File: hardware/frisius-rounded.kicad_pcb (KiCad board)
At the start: 4 copper layers, 50 x 50 mm, 117 parts, among them Q1 Q_NMOS_DGS, Q2 MBT2222ADW1T1, SW1 OVERRIDE, SW4 SW_Push, U1 ESP32-PICO-V3-02, U10 CP2102N-Axx-xQFN24, U12 RT5789, U2 FXOS8700CQR1, U3 MS5637-02BA03, U4 L96-M33, U5 MAX77751, U6 LM75B, U7 MAX17048G

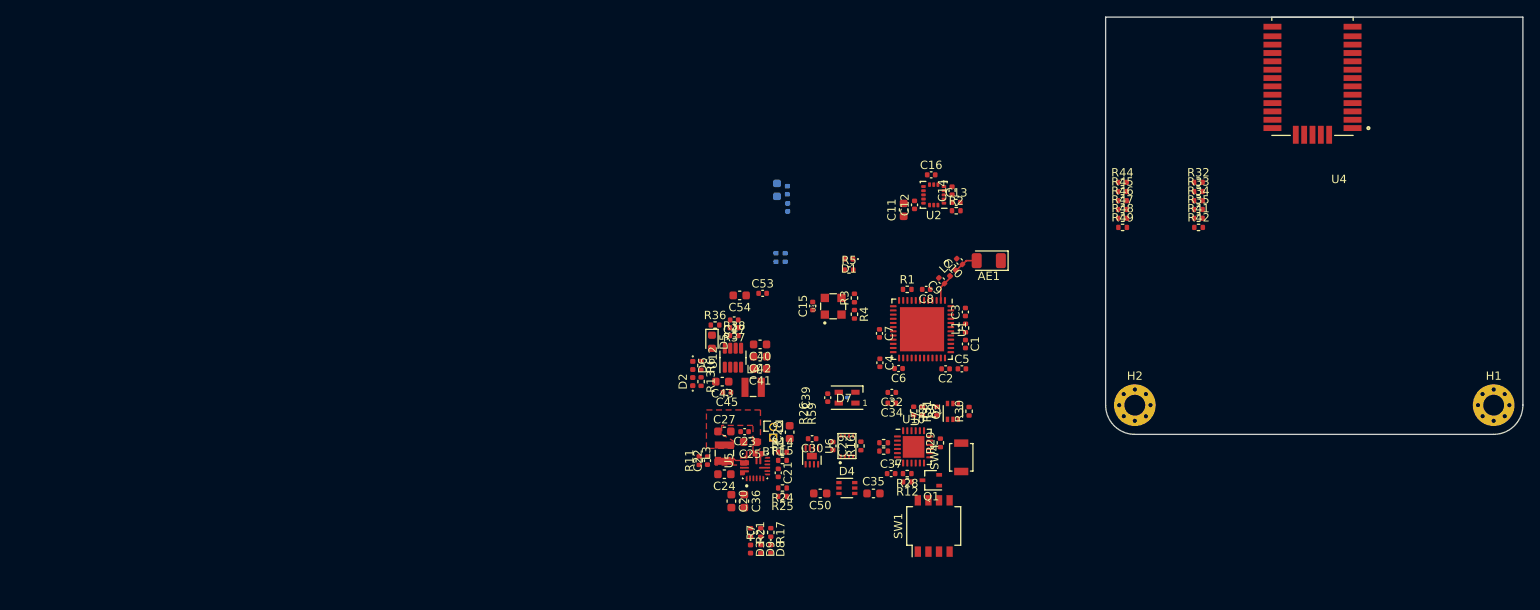
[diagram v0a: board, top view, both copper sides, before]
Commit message: layout 0 unconnected
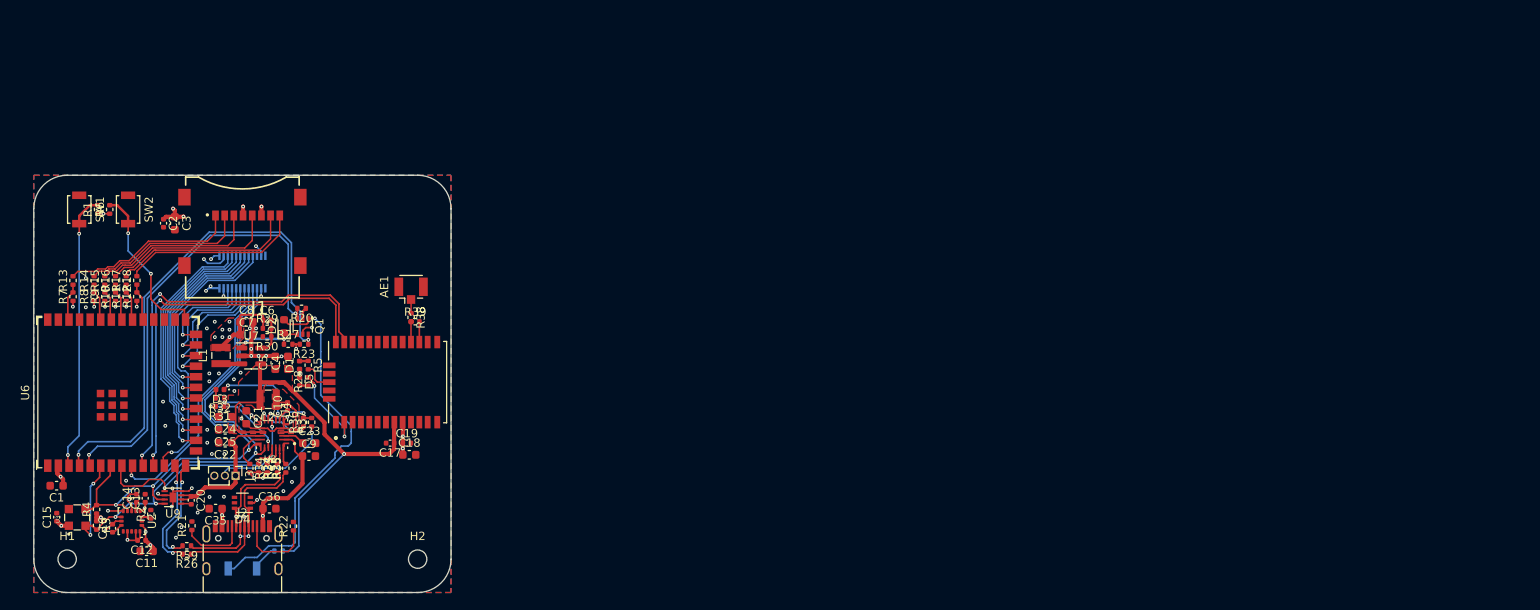
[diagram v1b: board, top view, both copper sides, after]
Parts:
- removed BT1: JST-PH-2, Connector_PinHeader_1.27mm:PinHeader_1x02_P1.27mm_Vertical
- removed C27, C28, C40, C41, C42: 10u, Capacitor_SMD:C_0603_1608Metric
- removed C29, C30, C37, C39, C53: 0.1u, Capacitor_SMD:C_0402_1005Metric
- removed C32, C34, C45: 1u, Capacitor_SMD:C_0402_1005Metric
- removed C43, C50, C54: 4.7u, Capacitor_SMD:C_0603_1608Metric
- removed C47: 10p, Capacitor_SMD:C_0402_1005Metric
- removed D6, D8, D9: LED_Small_Filled, LED_SMD:LED_0402_1005Metric
- removed D7: SK6805, LED_SMD:LED_SK6805_PLCC4_2.4x2.7mm_P1.3mm
- removed L3: 0.47u, Inductor_SMD:L_Wuerth_MAPI-2510
- removed L4: 1u, Inductor_SMD:L_Wuerth_MAPI-2510
- removed Q2: MBT2222ADW1T1, Package_TO_SOT_SMD:SOT-363_SC-70-6
- removed R41, R42: 22, Resistor_SMD:R_0402_1005Metric
- removed R44, R45, R46, R47, R48, R49: 10k, Resistor_SMD:R_0402_1005Metric
- removed SW4: SW_Push, Button_Switch_SMD:SW_SPST_B3U-1000P
- removed U1: ESP32-PICO-V3-02, Package_DFN_QFN:QFN-48-1EP_7x7mm_P0.5mm_EP5.3x5.3mm
- removed U10: CP2102N-Axx-xQFN24, Package_DFN_QFN:QFN-24-1EP_4x4mm_P0.5mm_EP2.6x2.6mm
- removed U12: RT5789, Package_TO_SOT_SMD:TSOT-23-8
- removed U5: MAX77751, bt_Package_QFN:FC2QFN-24-3x3_P0.4mm
- added J1: MEM2067, bt_Connector_uSD:GCT_MEM2067-02-180-00-A_REVB, F.Cu at (71.6, 90.9)
- added J2: USB_C_Receptacle_USB2.0, Connector_USB:USB_C_Receptacle_HRO_TYPE-C-31-M-12, F.Cu at (71.6, 129.6)
- added J3: BATTERY, Connector_PinHeader_1.27mm:PinHeader_1x03_P1.27mm_Vertical, F.Cu at (70.7, 119.5)
- added J4: Display, Connector_Molex:Molex_SlimStack_55560-0241_2x12_P0.50mm_Vertical, B.Cu at (71.6, 95.0)
- added R10: 10k, Resistor_SMD:R_0402_1005Metric, F.Cu at (56.4, 98.0)
- added R18: 22, Resistor_SMD:R_0402_1005Metric, F.Cu at (58.9, 96.0)
- added R19: 100k, Resistor_SMD:R_0402_1005Metric, B.Cu at (75.9, 128.5)
- added R20: 100k, Resistor_SMD:R_0402_1005Metric, F.Cu at (78.7, 99.4)
- added R22: 0, Resistor_SMD:R_0402_1005Metric, F.Cu at (77.7, 125.5)
- added R39: 0, Resistor_SMD:R_0402_1005Metric, F.Cu at (92.3, 101.0)
- added SW2: BOOT, Button_Switch_SMD:SW_SPST_B3U-1000P, F.Cu at (57.9, 87.5)
- added SW3: POWER, Button_Switch_SMD:SW_SPST_B3U-1000P, B.Cu at (71.6, 130.6)
- added U8: MP2723, bt_Package_QFN:MP_QFN-26-3.5x3.5_P0.45mm, F.Cu at (75.1, 114.5)
- added U9: MAX17048G, Package_DFN_QFN:TDFN-8-1EP_2x2mm_P0.5mm_EP0.8x1.2mm, F.Cu at (63.2, 122.0)
- AE1: value 2.4G -> Antenna_Shield; footprint RF_Antenna:Johanson_2450AT18x100 -> Connector_Coaxial:U.FL_Hirose_U.FL-R-SMT-1_Vertical
- C1, C3, C5, C9: value 0.1u -> 4.7u; footprint Capacitor_SMD:C_0402_1005Metric -> Capacitor_SMD:C_0603_1608Metric
- C17, C18, C19: moved to F.Cu
- C2: value 1u -> 0.1u
- C20: value 4.7u -> 0.1u; footprint Capacitor_SMD:C_0603_1608Metric -> Capacitor_SMD:C_0402_1005Metric
- C21, C23: value 1u -> 10u; footprint Capacitor_SMD:C_0402_1005Metric -> Capacitor_SMD:C_0603_1608Metric
- C22, C7, C8: value 0.1u -> 10u; footprint Capacitor_SMD:C_0402_1005Metric -> Capacitor_SMD:C_0603_1608Metric
- C4: value 1u -> 4.7u; footprint Capacitor_SMD:C_0402_1005Metric -> Capacitor_SMD:C_0603_1608Metric
- C6: value 0.1u -> 10p
- D2: value LED_Small_Filled -> MBR0540; footprint LED_SMD:LED_0402_1005Metric -> LED_SMD:LED_0603_1608Metric
- D5: value MBR0540 -> LED_Small_Filled; footprint LED_SMD:LED_0603_1608Metric -> LED_SMD:LED_0402_1005Metric
- H1, H2: footprint MountingHole:MountingHole_2.5mm_Pad_Via -> MountingHole:MountingHole_2.2mm_M2_ISO7380
- L1: value 0 -> 1u; footprint Resistor_SMD:R_0402_1005Metric -> Inductor_SMD:L_Wuerth_MAPI-2510
- L2: value L_Small -> 0.47u; footprint Inductor_SMD:L_0402_1005Metric -> Inductor_SMD:L_Wuerth_MAPI-2510
- N6: footprint Fiducial:Fiducial_0.5mm_Mask1.5mm -> Symbol:WEEE-Logo_4.2x6mm_SilkScreen
- Q1: value Q_NMOS_DGS -> Q_Dual_NMOS_G1S2G2D2S1D1; footprint Package_TO_SOT_SMD:SOT-323_SC-70 -> Package_TO_SOT_SMD:SOT-363_SC-70-6
- R1: value 100k -> R_Small
- R11, R12: value 100k -> 10k
- R13, R17: value 1k -> 22
- R14, R15: value 14k -> 22
- R16: value 0 -> 22
- R21: value 1k -> 0
- R23, R27: value 0 -> 100k; moved to F.Cu
- R28: value 100k -> 1k
- R29: value 100k -> ?
- R30: value 10k -> 100k
- R31: value 10k -> 1k
- R32: value 22 -> 1k
- R33, R34: value 22 -> 0
- R35: value 22 -> 14k
- R36: value 100k -> 14k
- R37: value ? -> 14k
- R38: value 100k -> 0
- R6: value 1k -> R_Small
- R7: value 1k -> 10k
- R8, R9: value 0 -> 10k
- SW1: value OVERRIDE -> RESET; footprint Button_Switch_SMD:SW_DIP_SPSTx04_Slide_Omron_A6H-4101_W6.15mm_P1.27mm -> Button_Switch_SMD:SW_SPST_B3U-1000P
- U6: value LM75B -> ESP32-S3-WROOM-1; footprint bt_Package_SON:XSON-8U -> bt_Espressif:ESP32-S3-WROOM-1U
- U7: value MAX17048G -> TLV62569DBV; footprint Package_DFN_QFN:TDFN-8-1EP_2x2mm_P0.5mm_EP0.8x1.2mm -> Package_TO_SOT_SMD:SOT-23-5
- moved H1 171.9 mm to (50.6, 129.4)
- moved R32 120.1 mm to (68.9, 110.2), turned to 180 degrees
- moved R34 118.1 mm to (72.5, 118.5), turned to -90 degrees
- moved R33 117.4 mm to (73.5, 118.5), turned to -90 degrees
- moved U4 116.7 mm to (89.0, 108.2), turned to 90 degrees
- moved R35 115.8 mm to (74.5, 118.6), turned to -90 degrees
- moved C1 110.2 mm to (49.3, 120.7), turned to 180 degrees
- moved SW1 109.2 mm to (52.0, 87.5), turned to -90 degrees
- moved C16 106.9 mm to (56.0, 125.8), turned to 90 degrees
- moved C14 104.4 mm to (58.9, 122.2)
- moved U2 103.8 mm to (58.3, 124.9), turned to -90 degrees
- moved C13 103.5 mm to (59.9, 122.2), turned to 90 degrees
- moved R2 103.1 mm to (60.6, 124.1), turned to 90 degrees
- moved N6 102.8 mm to (238.1, 68.7)
- moved C12 101.0 mm to (59.5, 127.2), turned to 180 degrees
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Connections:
- net /USB/PORT_D+ renamed /Power/PORT_D+
- net /USB/PORT_D- renamed /Power/PORT_D-
- AE1 pad 1: unconnected-(AE1-Pad1) -> /GPS/ANT_RF
- AE1 pad 2: Net-(AE1-Pad2) -> GND
- C1 pad 1: VDD_CORE_3V3 -> +3V3
- C10 pad 1: Net-(AE1-Pad2) -> Net-(C10-Pad1)
- C10 pad 2: GND -> Net-(C10-Pad2)
- C11 pad 1: VDD_AUX_3V3 -> +3V3
- C12 pad 1: VDD_AUX_3V3 -> +3V3
- C13 pad 1: Net-(C13-Pad1) -> +3V3
- C15 pad 1: VDD_AUX_3V3 -> +3V3
- C18 pad 1: VDD_AUX_3V3 -> +3V3
- C19 pad 1: VDD_AUX_3V3 -> +3V3
- C2 pad 1: VDD_CORE_3V3 -> +3V3
- C20 pad 1: VBUS -> +BATT
- C21 pad 1: Net-(C21-Pad1) -> /Power/VREF
- C22 pad 1: Net-(C22-Pad1) -> +BATT
- C22 pad 2: Net-(C22-Pad2) -> GND
- C24 pad 1: VBUS_OVP -> VDD_NVDC
- C3 pad 1: /Processor/3V3_ESP_VDDA_FILT -> +3V3
- C4 pad 1: VDD_CORE_3V3 -> VDD_NVDC
- C5 pad 1: VDD_CORE_3V3 -> VDD_NVDC
- C6 pad 1: Net-(C6-Pad1) -> +3V3
- C6 pad 2: GND -> Net-(C6-Pad2)
- C7 pad 1: VDD_CORE_3V3 -> +3V3
- C8 pad 1: /Processor/3V3_ESP_VDDA_FILT -> +3V3
- C9 pad 1: Net-(C9-Pad1) -> VBUS
- D2 pad 2: VDD_NVDC -> Net-(D2-Pad2)
- D3 pad 2: VDD_NVDC -> Net-(D3-Pad2)
- D4 pad 3: /BMS/USB_CC.1 -> unconnected-(D4-Pad3)
- D4 pad 4: /BMS/USB_CC.2 -> unconnected-(D4-Pad4)
- D5 pad 1: /Power/POWER_EN -> GND
- D5 pad 2: /Power/BOOTSTRAP -> Net-(D5-Pad2)
- L1 pad 1: VDD_CORE_3V3 -> Net-(L1-Pad1)
- L1 pad 2: /Processor/3V3_ESP_VDDA_FILT -> +3V3
- L2 pad 1: Net-(C9-Pad1) -> Net-(C10-Pad2)
- L2 pad 2: Net-(AE1-Pad2) -> VDD_NVDC
- Q1 pad 1: /Processor/USB_PRESENT -> Net-(D2-Pad2)
- Q1 pad 2: Net-(Q1-Pad2) -> GND
- Q1 pad 3: GND -> /Power/SHUTDOWN
- R1 pad 1: VDD_CORE_3V3 -> +3V3
- R1 pad 2: /Processor/DEV_BTN.RST -> /Processor/RST_BTN
- R11 pad 1: Net-(Q1-Pad2) -> +3V3
- R11 pad 2: VDD_NVDC -> /Processor/SDMMC.D0
- R12 pad 1: /Processor/USB_PRESENT -> +3V3
- R12 pad 2: VDD_CORE_3V3 -> /Processor/SDMMC.D1
- R13 pad 1: Net-(Q1-Pad2) -> /Processor/SDMMC.D2
- R13 pad 2: Net-(D2-Pad1) -> Net-(J1-Pad1)
- R14 pad 1: Net-(R14-Pad1) -> /Processor/SDMMC.D3
- R14 pad 2: GND -> Net-(J1-Pad2)
- R15 pad 1: Net-(R15-Pad1) -> /Processor/SDMMC.CMD
- R15 pad 2: GND -> Net-(J1-Pad3)
- R16 pad 1: /BMS/THERM_SHDN -> /Processor/SDMMC.CLK
- R16 pad 2: Net-(R15-Pad1) -> Net-(J1-Pad5)
- R17 pad 1: Net-(D8-Pad1) -> /Processor/SDMMC.D0
- R21 pad 2: Net-(D3-Pad1) -> GND
- R23 pad 1: Net-(R23-Pad1) -> /Power/POWER_BUTTON
- R23 pad 2: /BMS/SENSOR_I2C.SDA -> +3V3
- R24 pad 2: /BMS/USB_CHG.D- -> /Power/USB_CHG.D-
- R25 pad 2: /BMS/USB_CHG.D+ -> /Power/USB_CHG.D+
- R26 pad 2: /USB/CP2102N_D- -> /Power/USB_ESP.D-
- R27 pad 1: Net-(R27-Pad1) -> Net-(D2-Pad1)
- R27 pad 2: /BMS/SENSOR_I2C.SCL -> +3V3
- R28 pad 1: Net-(R28-Pad1) -> Net-(D5-Pad2)
- R28 pad 2: VDD_CORE_3V3 -> /GPS/L96_FIX
- R29 pad 1: /USB/CP2102N_~{SUS} -> +3V3
- R29 pad 2: GND -> Net-(C6-Pad2)
- R3 pad 1: VDD_AUX_3V3 -> +3V3
- R3 pad 2: /BMS/SENSOR_I2C.SDA -> /Display/SYS_I2C.SDA
- R30 pad 1: /USB/~{RTS}_BASE -> Net-(C6-Pad2)
- R30 pad 2: /USB/CP2102N_RTS -> GND
- R31 pad 1: /USB/CP2102N_DTR -> /Power/VREF
- R31 pad 2: /USB/DTR_BASE -> Net-(R31-Pad2)
- R32 pad 1: /Processor/SDMMC.D2 -> /Power/VREF
- R32 pad 2: Net-(J4-Pad1) -> Net-(D3-Pad2)
- R33 pad 1: /Processor/SDMMC.D3 -> Net-(R33-Pad1)
- R33 pad 2: Net-(J4-Pad2) -> GND
- R34 pad 1: /Processor/SDMMC.CMD -> Net-(R34-Pad1)
- R34 pad 2: Net-(J4-Pad3) -> GND
- R35 pad 1: /Processor/SDMMC.CLK -> Net-(R35-Pad1)
- R35 pad 2: Net-(J4-Pad5) -> GND
- R36 pad 1: /Power/POWER_EN -> Net-(R36-Pad1)
- R36 pad 2: VDD_SYS_3V5 -> Net-(R36-Pad2)
- R37 pad 1: VDD_SYS_3V5 -> Net-(J3-Pad2)
- R37 pad 2: Net-(C47-Pad2) -> Net-(R36-Pad2)
- R38 pad 1: Net-(C47-Pad2) -> /GPS/ANT_RF
- R38 pad 2: GND -> /GPS/GPS_RF
- R4 pad 1: VDD_AUX_3V3 -> +3V3
- R4 pad 2: /BMS/SENSOR_I2C.SCL -> /Display/SYS_I2C.SCL
- R59 pad 2: /USB/CP2102N_D+ -> /Power/USB_ESP.D+
- R6 pad 1: Net-(D6-Pad1) -> +3V3
- R6 pad 2: Net-(R6-Pad2) -> /Processor/BOOT_BTN
- R7 pad 1: Net-(D9-Pad1) -> +3V3
- R7 pad 2: Net-(R7-Pad2) -> /Processor/SDMMC.D2
- R8 pad 1: /Processor/DEBUG_UART.RXD -> +3V3
- R8 pad 2: /USB/CP2102N_UART_TX -> /Processor/SDMMC.D3
- R9 pad 1: /Processor/DEBUG_UART.TXD -> +3V3
- R9 pad 2: /USB/CP2102N_UART_RX -> /Processor/SDMMC.CMD
- SW1 pad 1: unconnected-(SW1-Pad1) -> GND
- SW1 pad 2: unconnected-(SW1-Pad2) -> /Processor/RST_BTN
- U2 pad 1: Net-(C13-Pad1) -> +3V3
- U2 pad 14: VDD_AUX_3V3 -> +3V3
- U2 pad 4: /BMS/SENSOR_I2C.SCL -> /Display/SYS_I2C.SCL
- U2 pad 6: /BMS/SENSOR_I2C.SDA -> /Display/SYS_I2C.SDA
- U3 pad 1: VDD_AUX_3V3 -> +3V3
- U3 pad 2: /BMS/SENSOR_I2C.SDA -> /Display/SYS_I2C.SDA
- U3 pad 3: /BMS/SENSOR_I2C.SCL -> /Display/SYS_I2C.SCL
- U4 pad 16: /GPS/GPS_RF -> /GPS/MOD_RF
- U4 pad 2: Net-(TP11-Pad1) -> /GPS/L96_FIX
- U4 pad 3: Net-(R23-Pad1) -> unconnected-(U4-Pad3)
- U4 pad 6: Net-(R27-Pad1) -> unconnected-(U4-Pad6)
- U4 pad 9: VDD_AUX_3V3 -> +3V3
- U6 pad 1: /BMS/SENSOR_I2C.SDA -> GND
- U6 pad 2: /BMS/SENSOR_I2C.SCL -> +3V3
- U6 pad 3: /BMS/THERM_SHDN -> /Processor/RST_BTN
- U6 pad 4: GND -> /Power/POWER_BUTTON
- U6 pad 5: GND -> /Power/SHUTDOWN
- U6 pad 6: GND -> /Display/SYS_I2C.SDA
- U6 pad 7: GND -> /Display/SYS_I2C.SCL
- U6 pad 8: +BATT -> /Power/BMS_INT
- U7 pad 1: GND -> Net-(D2-Pad1)
- U7 pad 2: +BATT -> GND
- U7 pad 3: +BATT -> Net-(L1-Pad1)
- U7 pad 4: GND -> VDD_NVDC
- U7 pad 5: unconnected-(U7-Pad5) -> Net-(C6-Pad2)
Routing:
- net /Display/SYS_I2C.SDA: track 0.00 -> 65.2 mm, vias 0 -> 5
- net /Power/POWER_BUTTON: track 0.00 -> 61.9 mm, vias 0 -> 2
- net /Display/SYS_I2C.SCL: track 0.00 -> 59.4 mm, vias 0 -> 3
- net /Power/SHUTDOWN: track 0.00 -> 56.1 mm, vias 0 -> 2
- net GND: track 0.00 -> 53.6 mm, vias 0 -> 53
- net VDD_NVDC: track 0.00 -> 52.7 mm, vias 0 -> 1
- net /GPS/GPS_UART.RX: track 0.00 -> 48.9 mm, vias 0 -> 2
- net /GPS/GPS_UART.TX: track 0.00 -> 46.6 mm, vias 0 -> 2
- net Net-(D2-Pad2): track 0.00 -> 45.7 mm, vias 0 -> 1
- net +3V3: track 0.00 -> 44.5 mm, vias 0 -> 29
- net /Processor/RST_BTN: track 0.00 -> 33.3 mm, vias 0 -> 2
- net /Display/TOUCH_INT: track 0.00 -> 31.6 mm, vias 0 -> 1
- net /Display/DISPLAY_BL: track 0.00 -> 29.5 mm, vias 0 -> 1
- net /Display/LCD_SPI_CTRL: track 0.00 -> 29.1 mm, vias 0 -> 1
- net /Display/RGB.R0: track 0.00 -> 28.3 mm, vias 0 -> 1
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- added copper zone on F.Cu, net +3V3
- added copper zone on In2.Cu, net +3V3
- added copper zone on B.Cu, net GND
- added copper zone on F.Cu, net GND
- added copper zone on In1.Cu, net GND
- added copper zone on F.Cu, net Net-(C10-Pad2)
- removed copper zone on F.Cu, net Net-(C22-Pad2)
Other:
- outline, holes or cut-outs redrawn
- rule pad_to_mask_clearance: 0.05 -> 0
- board text removed: "AUX"
- board text removed: "BATT"
- board text removed: "NVDC"
- board text removed: "SYS"
- board text removed: "VBUS"
